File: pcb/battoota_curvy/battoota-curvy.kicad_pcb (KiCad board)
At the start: 2 copper layers, 128.3 x 99.3 mm, 38 parts

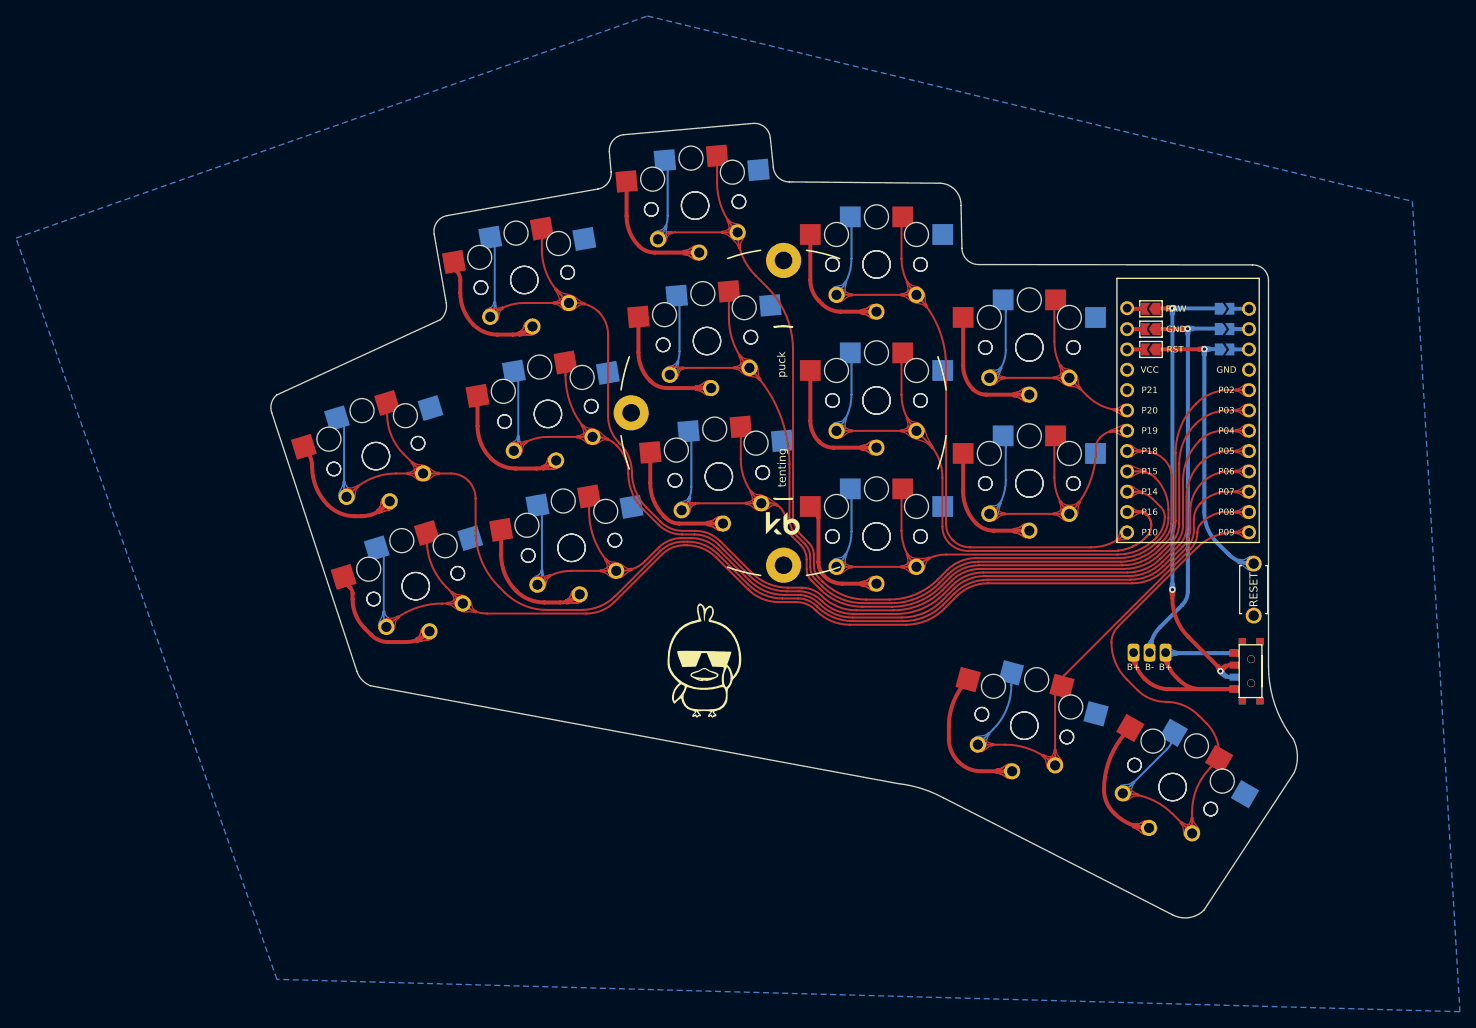
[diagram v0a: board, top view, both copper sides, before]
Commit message: fix gnd  issue in 30 keys
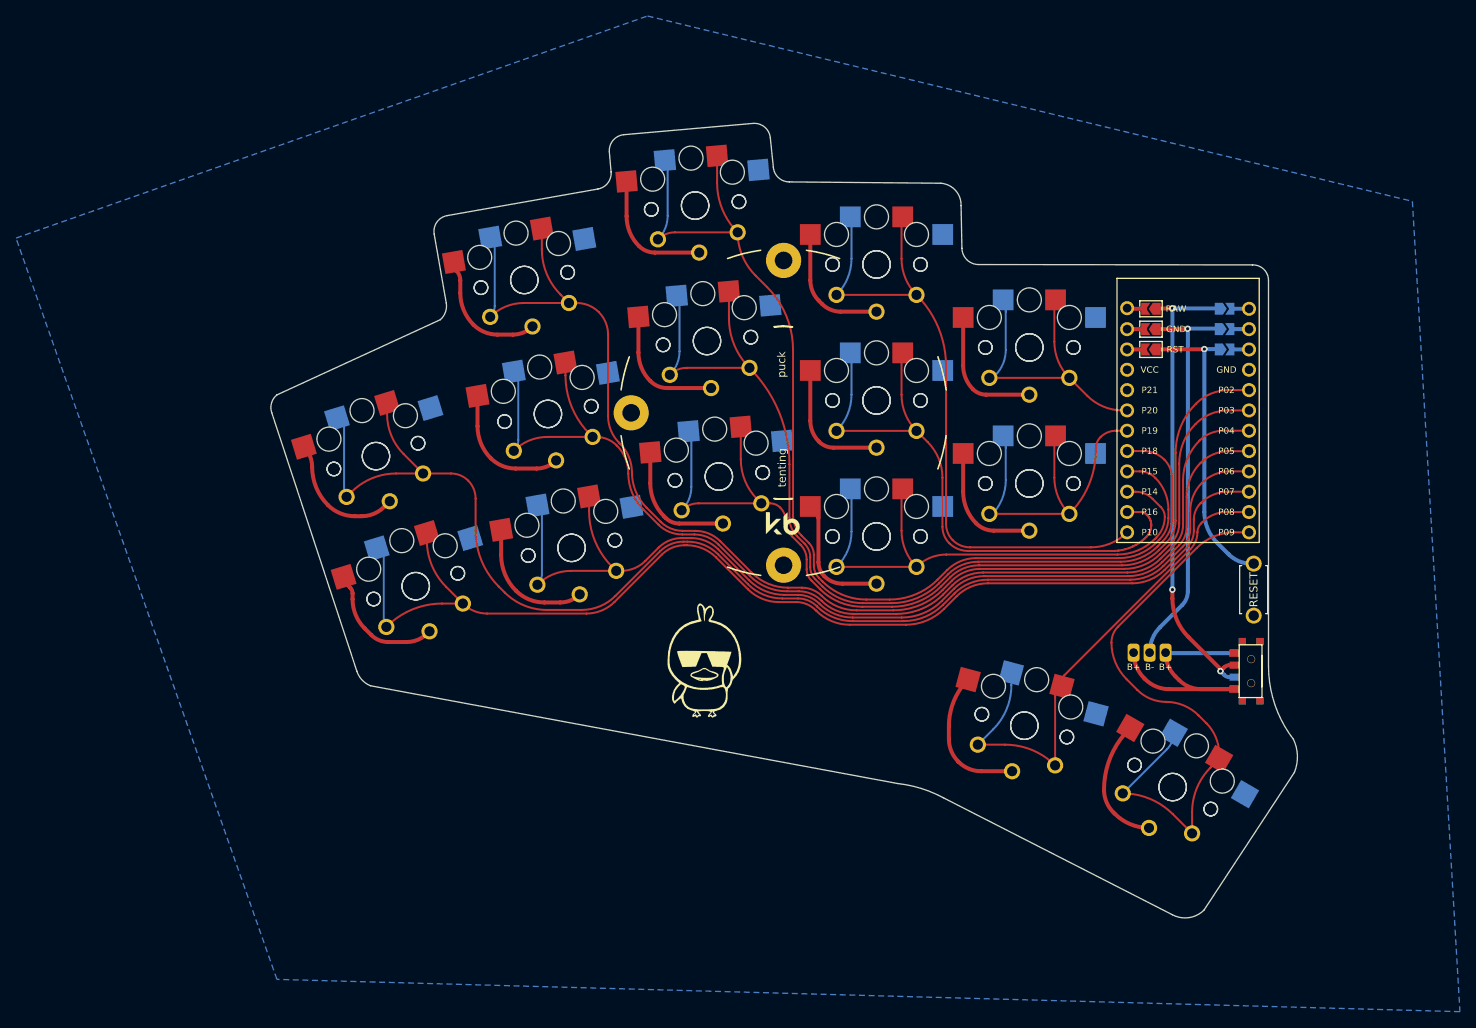
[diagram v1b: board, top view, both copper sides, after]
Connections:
- MCU1 pad 16: GND -> (no net)
- MCU1 pad 2: Bgnd -> GND
- PAD1 pad 2: Bgnd -> GND
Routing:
- net GND: track 248.9 -> 298.8 mm, vias 0 -> 1
- net Bgnd: track 49.9 -> 0.00 mm, vias 1 -> 0
